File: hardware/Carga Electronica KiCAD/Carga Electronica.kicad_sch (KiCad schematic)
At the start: 51 parts, among them J1 SHUNT, J2 ACS712, J3 LM35, J4 LCD_3310, J5 ENCODER, J6 Vin, J7 BATTERY, J8 COOLER FAN, M1 Fan, Q1 IRF540N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

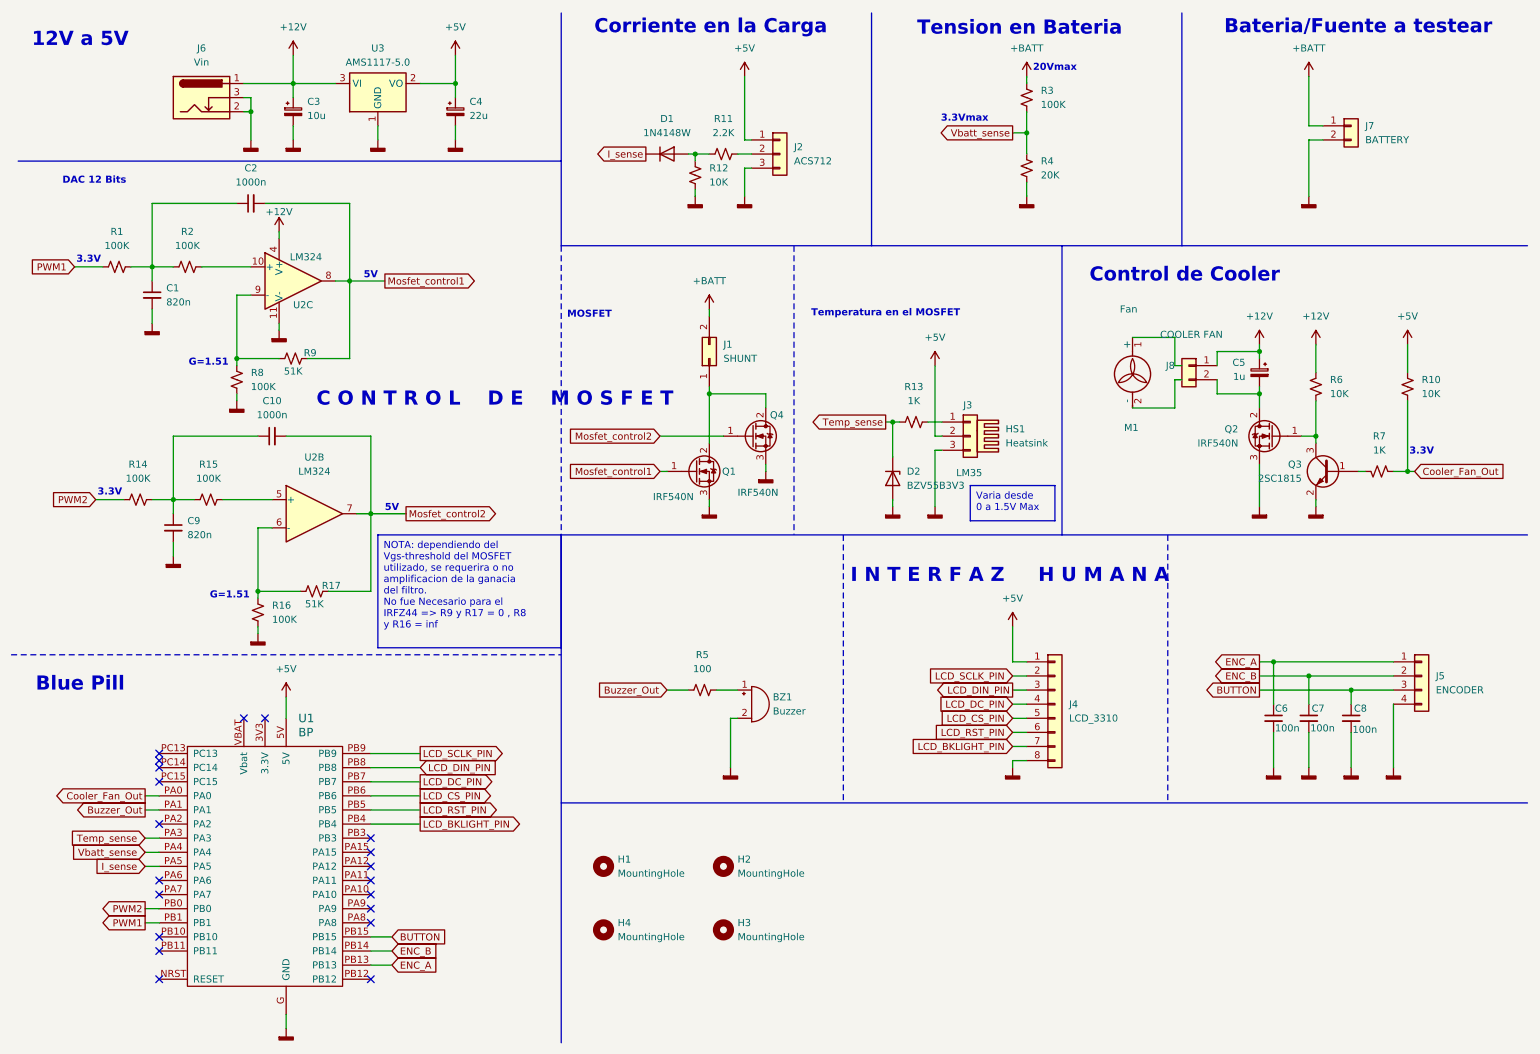
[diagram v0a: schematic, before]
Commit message: Se cambio el divisor resistivo por R de precision
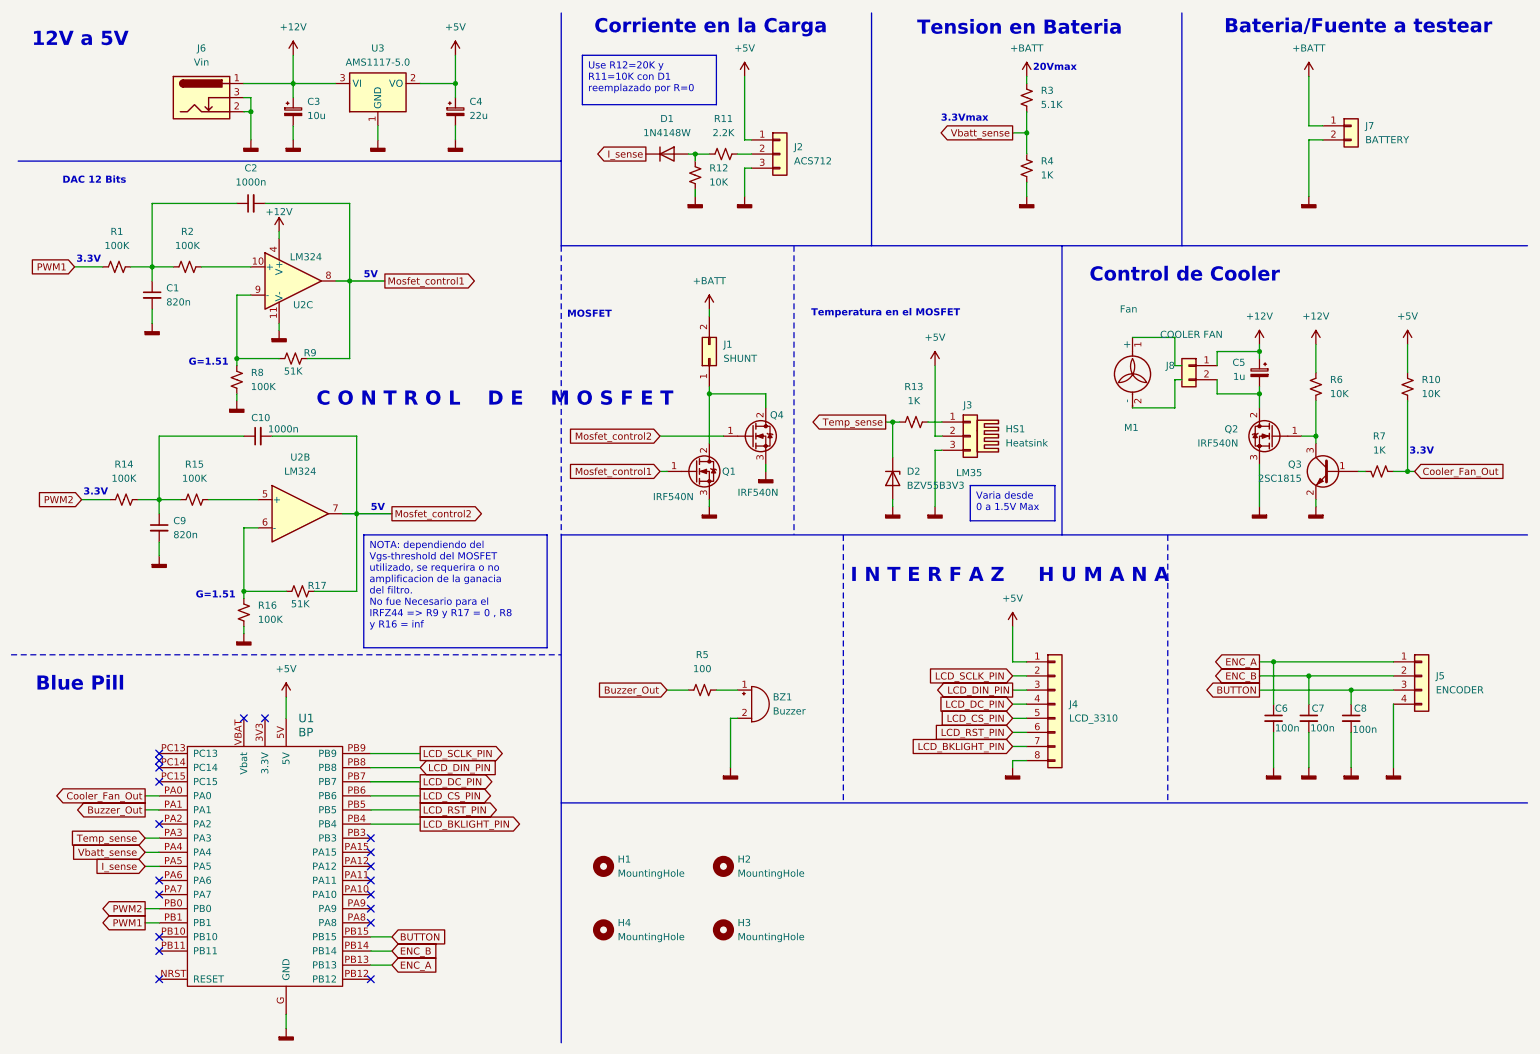
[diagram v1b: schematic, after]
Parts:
- R3: value 100K -> 5.1K
- R4: value 20K -> 1K
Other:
- moved on the sheet: C10, C9, R14, R15, R16, R17, U2B
